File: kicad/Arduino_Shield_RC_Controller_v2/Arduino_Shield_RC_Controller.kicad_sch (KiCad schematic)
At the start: 13 parts, among them J1 CONN_04X2, SW1 PTS810SJG250SMTRLFS, SW2 PTS810SJG250SMTRLFS, SW3 PTS810SJG250SMTRLFS, SW4 PTS810SJG250SMTRLFS, SW5 PTS810SJG250SMTRLFS, SW6 SW_Omron_B3FS

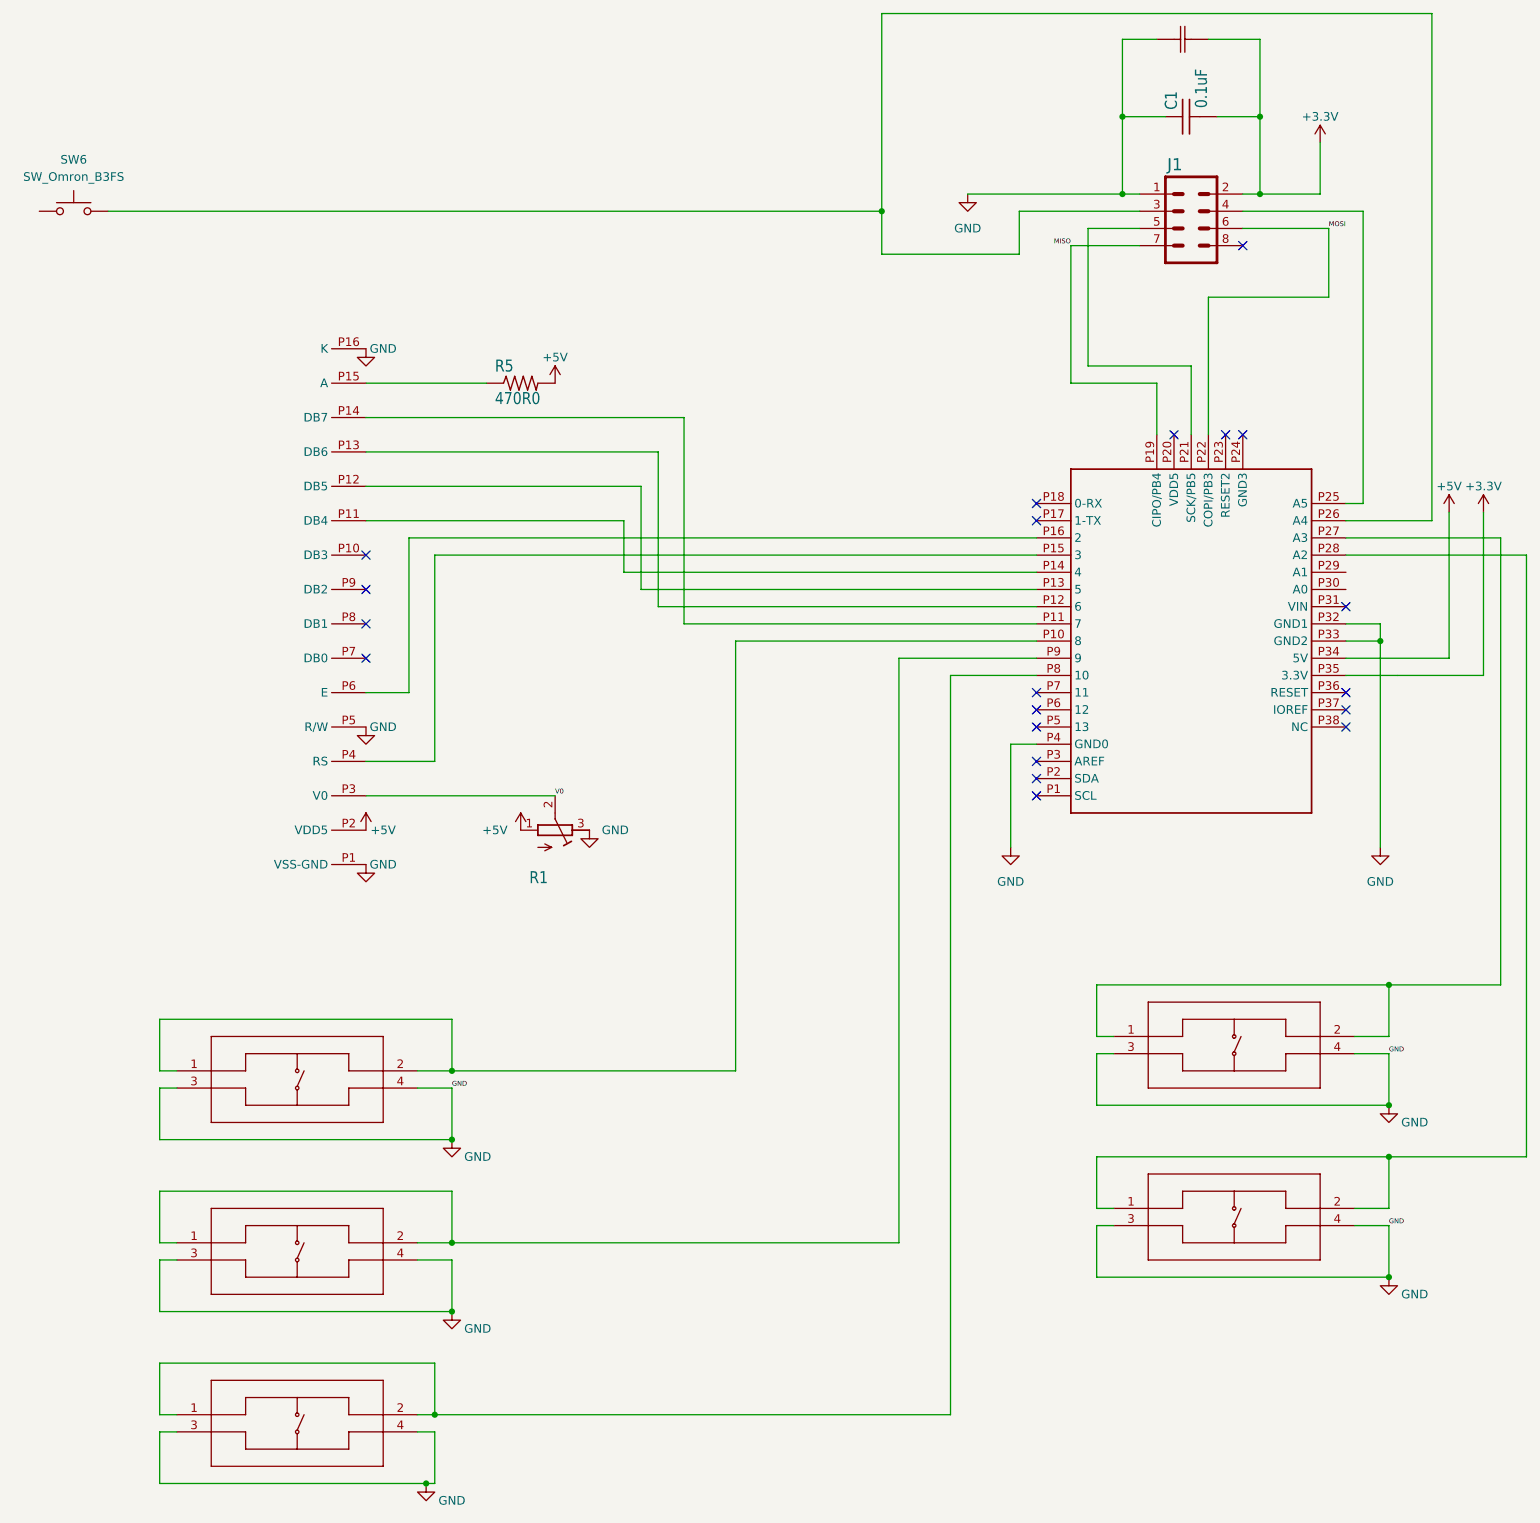
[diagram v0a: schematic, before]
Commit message: starting the Hobby RC and Motor Control shield
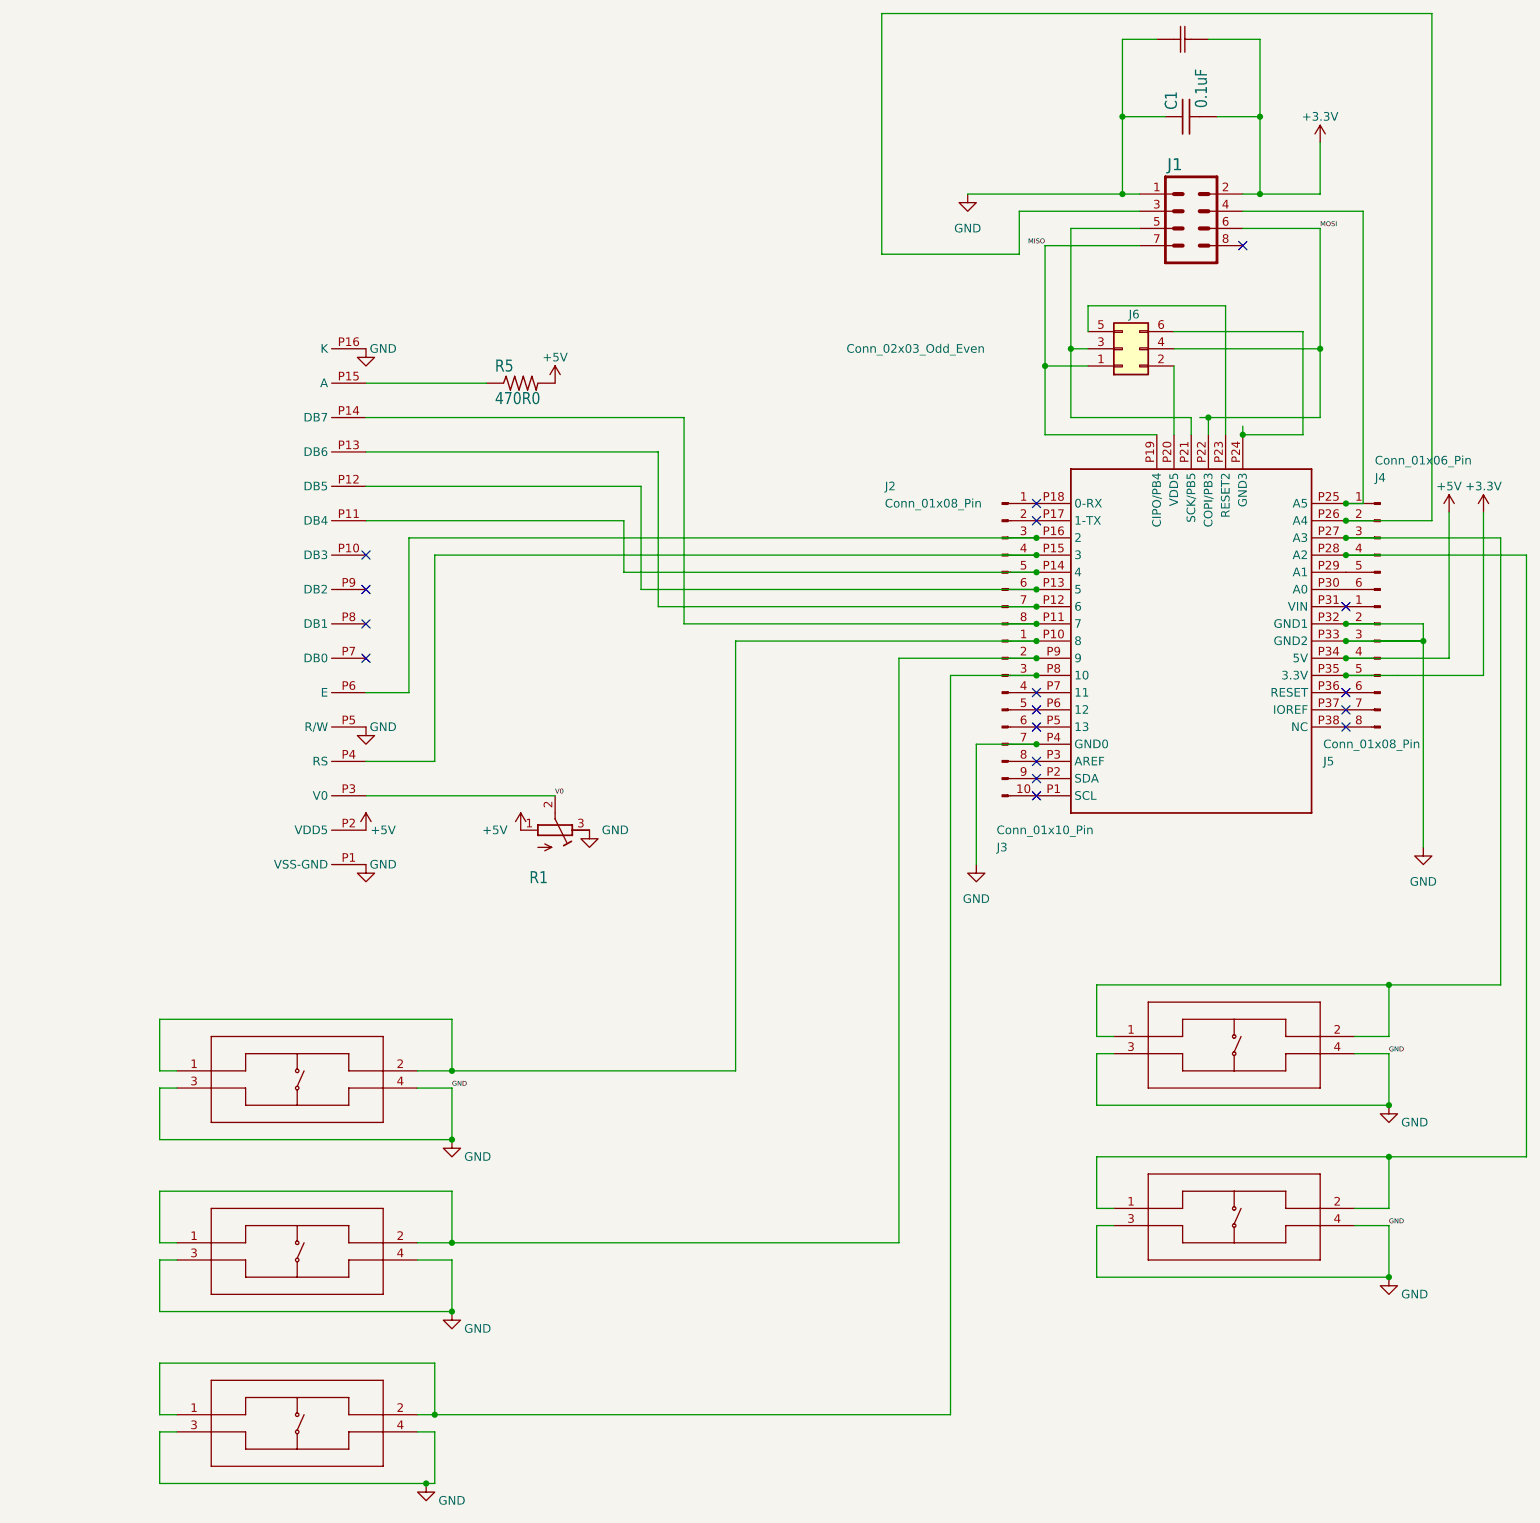
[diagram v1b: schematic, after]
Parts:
- removed SW6: SW_Omron_B3FS, Button_Switch_THT:SW_TH_Tactile_Omron_B3F-10xx, symbol Switch:SW_Omron_B3FS
- added J2, J5: Conn_01x08_Pin, Connector_PinHeader_2.54mm:PinHeader_1x08_P2.54mm_Vertical, symbol Connector:Conn_01x08_Pin
- added J3: Conn_01x10_Pin, Connector_PinHeader_2.54mm:PinHeader_1x10_P2.54mm_Vertical, symbol Connector:Conn_01x10_Pin
- added J4: Conn_01x06_Pin, Connector_PinHeader_2.54mm:PinHeader_1x06_P2.54mm_Vertical, symbol Connector:Conn_01x06_Pin
- added J6: Conn_02x03_Odd_Even, Connector_PinSocket_2.54mm:PinSocket_2x03_P2.54mm_Vertical, symbol Connector_Generic:Conn_02x03_Odd_Even
- R1: footprint Arduino_Shield_RC_Controller:RTRIM3103 -> Potentiometer_THT:Potentiometer_Runtron_RM-065_Vertical
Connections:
- net +3.3V: now also J5.5 (Pin_5)
- net +5V: now also J5.4 (Pin_4)
- net GND: now also J3.7 (Pin_7), J5.2 (Pin_2), J5.3 (Pin_3)
- net MISO: now also J6.1 (Pin_1)
- net MOSI: now also J6.4 (Pin_4)
- net at AR1.P14 (4), LCD1.P11 (DB4): now also J2.5 (Pin_5)
- net at AR1.P13 (5), LCD1.P12 (DB5): now also J2.6 (Pin_6)
- net at AR1.P12 (6), LCD1.P13 (DB6): now also J2.7 (Pin_7)
- net at AR1.P11 (7), LCD1.P14 (DB7): now also J2.8 (Pin_8)
- net at AR1.P15 (3), LCD1.P4 (RS): now also J2.4 (Pin_4)
- net at AR1.P16 (2), LCD1.P6 (E): now also J2.3 (Pin_3)
- net at AR1.P26 (A4), J1.3: now also J4.2 (Pin_2)
- net at AR1.P28 (A2), SW5.1, SW5.2: now also J4.4 (Pin_4)
- net at AR1.P1 (SCL): now also J3.10 (Pin_10)
- net at AR1.P10 (8), SW1.1, SW1.2: now also J3.1 (Pin_1)
- net at AR1.P17 (1-TX): now also J2.2 (Pin_2)
- net at AR1.P18 (0-RX): now also J2.1 (Pin_1)
- net at AR1.P2 (SDA): now also J3.9 (Pin_9)
- net at AR1.P20 (VDD5): now also J6.2 (Pin_2)
- net at AR1.P21 (SCK/PB5), J1.5: now also J6.3 (Pin_3)
- net at AR1.P23 (RESET2): now also J6.5 (Pin_5)
- net at AR1.P24 (GND3): now also J6.6 (Pin_6)
- net at AR1.P25 (A5), J1.4: now also J4.1 (Pin_1)
- net at AR1.P27 (A3), SW4.1, SW4.2: now also J4.3 (Pin_3)
- net at AR1.P29 (A1): now also J4.5 (Pin_5)
- net at AR1.P3 (AREF): now also J3.8 (Pin_8)
- net at AR1.P30 (A0): now also J4.6 (Pin_6)
- net at AR1.P31 (VIN): now also J5.1 (Pin_1)
- net at AR1.P36 (RESET): now also J5.6 (Pin_6)
- net at AR1.P37 (IOREF): now also J5.7 (Pin_7)
- net at AR1.P38 (NC): now also J5.8 (Pin_8)
- net at AR1.P5 (13): now also J3.6 (Pin_6)
- net at AR1.P6 (12): now also J3.5 (Pin_5)
- net at AR1.P7 (11): now also J3.4 (Pin_4)
- net at AR1.P8 (10), SW3.1, SW3.2: now also J3.3 (Pin_3)
- net at AR1.P9 (9), SW2.1, SW2.2: now also J3.2 (Pin_2)
- no-connect marks 20 -> 17
